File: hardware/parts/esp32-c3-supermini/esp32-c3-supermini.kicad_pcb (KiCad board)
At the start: 2 copper layers, 18 x 22.5 mm, 2 parts, among them J1 Conn_01x08, J2 Conn_01x08

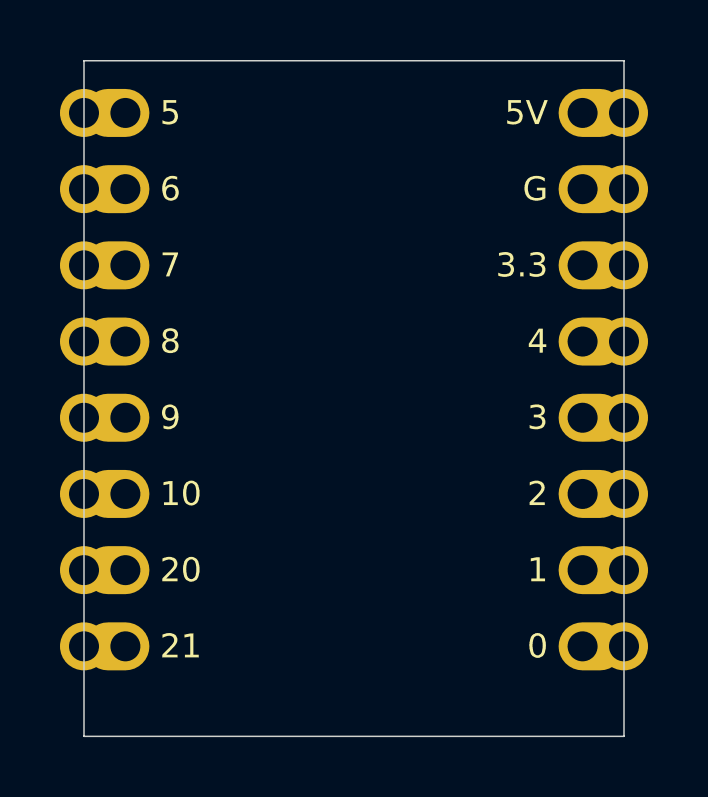
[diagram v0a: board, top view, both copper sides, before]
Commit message: Silk: "3V3" instead of "3.3", and the UART pins named on the spare header
The 3.3 V pin is labelled 3V3 on the SuperMini board and beside the
SuperMini on the adapters, and the expansion header's GPIO21/20 pins read
"21TX" / "20RX".

Co-Authored-By: Claude Fable 5.1 <noreply@anthropic.com>
Claude-Session: https://claude.ai/code/session_01JoGdh4Cg3VtTTDZi4gQuiN
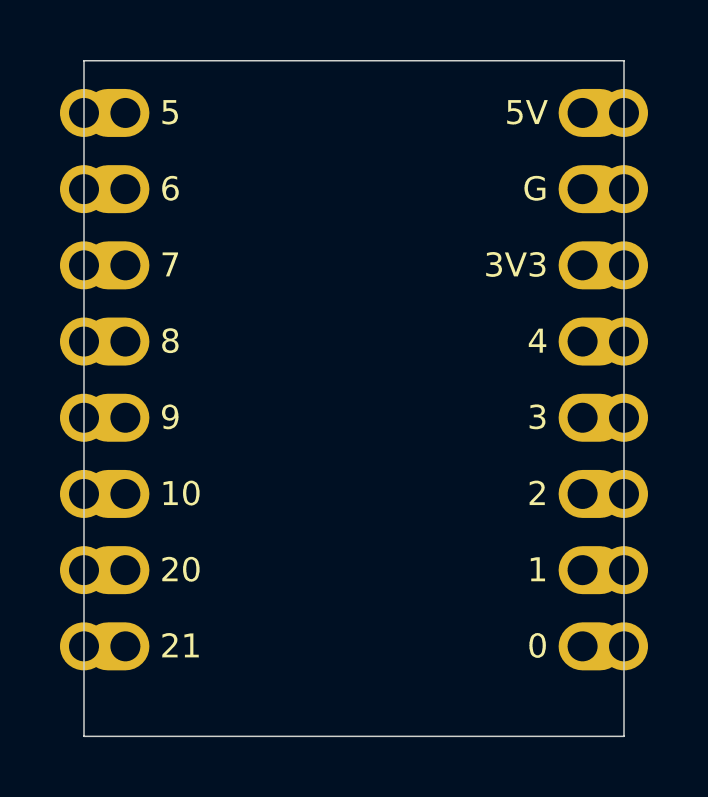
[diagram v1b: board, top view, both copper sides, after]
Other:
- board text added: "3V3"
- board text removed: "3.3"
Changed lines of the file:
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@@
 		)
 	)
-	(gr_text "3.3"
+	(gr_text "3V3"
 		(at 115.47 106.82 0)
 		(layer "F.SilkS")
@@
 		)
 	)
-	(gr_text "3.3"
+	(gr_text "3V3"
 		(at 115.47 106.82 0)
 		(layer "B.SilkS")
